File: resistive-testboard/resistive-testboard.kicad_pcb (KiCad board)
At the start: 2 copper layers, 34 parts, among them J1 Conn_01x04_Pin, Q1 PMOS, Q2 PMOS, Q3 PMOS, Q4 PMOS, Q5 PMOS, Q6 PMOS

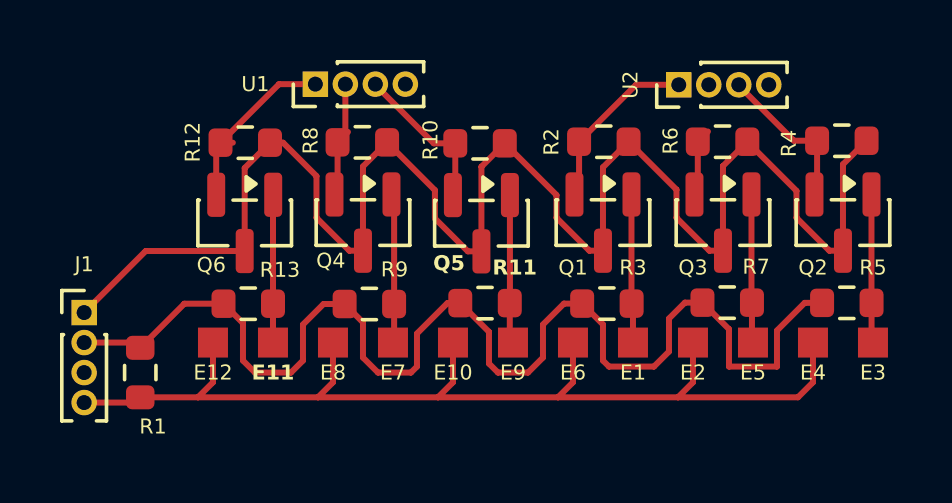
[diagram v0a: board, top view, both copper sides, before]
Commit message: fixed pinouts for ws2811 and pmos
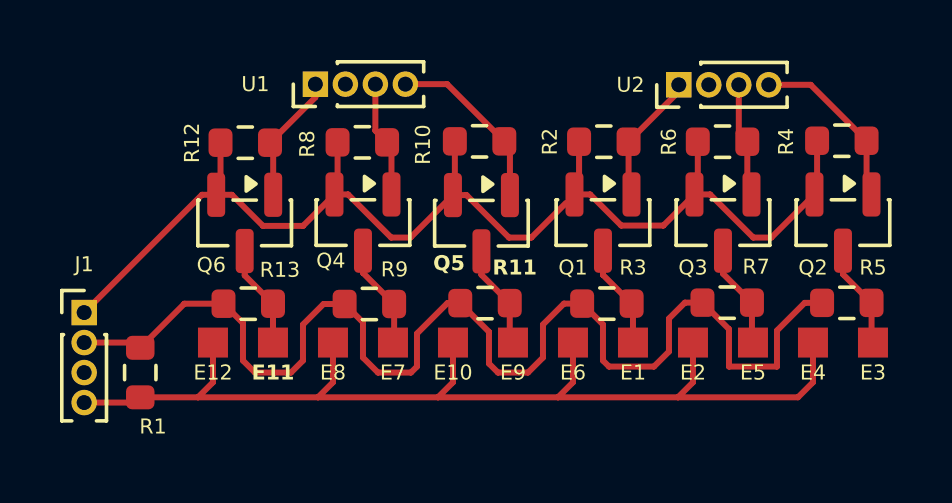
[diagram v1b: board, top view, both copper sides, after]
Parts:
- moved R10 0.07 mm to (138.9, 81.8), turned to 0 degrees
- turned R12 to 0 degrees
- turned R2 to 0 degrees
- turned R4 to 0 degrees
- turned R6 to 0 degrees
- turned R8 to 0 degrees
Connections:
- Q1 pad 1: Net-(E1-E) -> /M1/S1/SIG_IN
- Q1 pad 2: /M1/S1/SIG_IN -> /V_SIG
- Q1 pad 3: /V_SIG -> Net-(E1-E)
- Q2 pad 1: Net-(E3-E) -> /M1/S3/SIG_IN
- Q2 pad 2: /M1/S3/SIG_IN -> /V_SIG
- Q2 pad 3: /V_SIG -> Net-(E3-E)
- Q3 pad 1: Net-(E5-E) -> /M1/S2/SIG_IN
- Q3 pad 2: /M1/S2/SIG_IN -> /V_SIG
- Q3 pad 3: /V_SIG -> Net-(E5-E)
- Q4 pad 1: Net-(E7-E) -> /M2/S2/SIG_IN
- Q4 pad 2: /M2/S2/SIG_IN -> /V_SIG
- Q4 pad 3: /V_SIG -> Net-(E7-E)
- Q5 pad 1: Net-(E9-E) -> /M2/S3/SIG_IN
- Q5 pad 2: /M2/S3/SIG_IN -> /V_SIG
- Q5 pad 3: /V_SIG -> Net-(E9-E)
- Q6 pad 1: Net-(E11-E) -> /M2/S1/SIG_IN
- Q6 pad 2: /M2/S1/SIG_IN -> /V_SIG
- Q6 pad 3: /V_SIG -> Net-(E11-E)
- U1 pad 2: /M2/S2/SIG_IN -> unconnected-(U1-VDD_OUT-Pad2)
- U1 pad 3: /M2/S3/SIG_IN -> /M2/S2/SIG_IN
- U1 pad 4: unconnected-(U1-VDD_OUT-Pad4) -> /M2/S3/SIG_IN
- U2 pad 2: /M1/S2/SIG_IN -> unconnected-(U2-VDD_OUT-Pad2)
- U2 pad 3: /M1/S3/SIG_IN -> /M1/S2/SIG_IN
- U2 pad 4: unconnected-(U2-VDD_OUT-Pad4) -> /M1/S3/SIG_IN
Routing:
- net /V_SIG: track 56.2 -> 42.8 mm
- net /M2/S1/SIG_IN: track 6.33 -> 4.37 mm
- net Net-(E7-E): track 5.14 -> 3.56 mm
- net /M1/S2/SIG_IN: track 2.28 -> 3.83 mm
- net /M1/S1/SIG_IN: track 5.93 -> 4.39 mm
- net Net-(E11-E): track 6.23 -> 4.74 mm
- net Net-(E1-E): track 4.96 -> 3.48 mm
- net Net-(E5-E): track 4.96 -> 3.48 mm
- net Net-(E3-E): track 4.96 -> 3.48 mm
- net Net-(E9-E): track 5.11 -> 3.64 mm
- net /M1/S3/SIG_IN: track 5.22 -> 5.89 mm
- net /M2/S3/SIG_IN: track 5.45 -> 5.96 mm

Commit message: added pcb?
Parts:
- J1: footprint Connector_PinHeader_1.00mm:PinHeader_1x04_P1.00mm_Vertical -> Connector_PinHeader_2.54mm:PinHeader_1x04_P2.54mm_Vertical
- moved J1 3.09 mm to (124.0, 84.9)
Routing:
- net RX: track 36.3 -> 38.9 mm
- net GND: track 41.5 -> 43.6 mm
- net /V_SIG: track 42.8 -> 43.9 mm

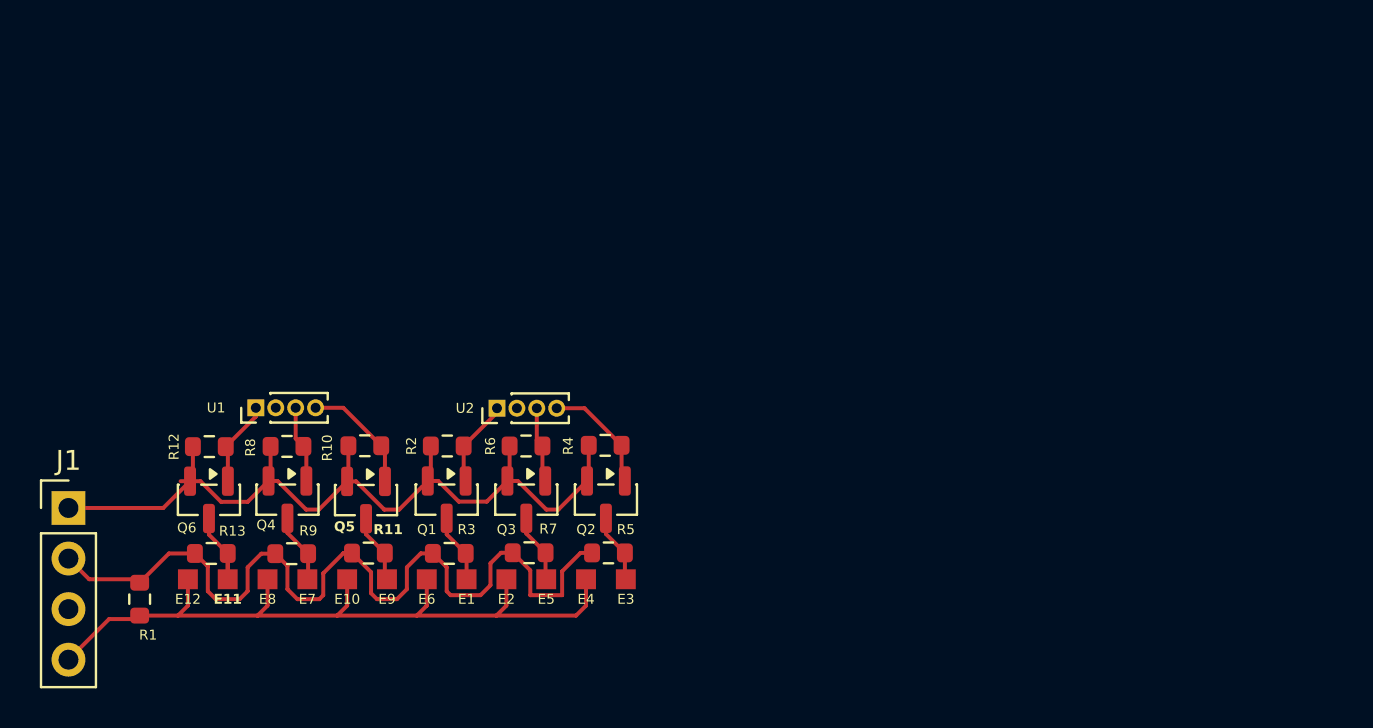
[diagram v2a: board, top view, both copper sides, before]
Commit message: moved pulldown resistor lower, added more copies of symbol
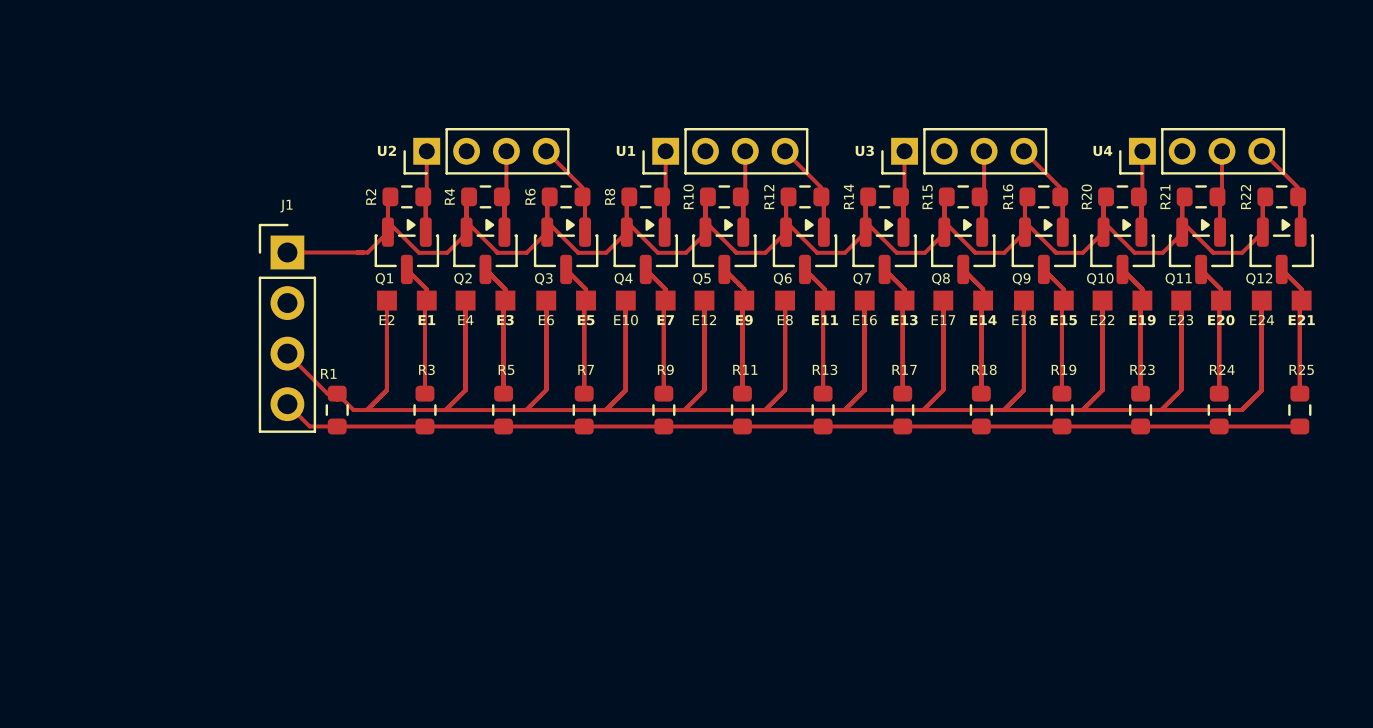
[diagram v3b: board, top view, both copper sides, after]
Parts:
- removed the E7 at (136.0, 88.5)
- removed the E8 at (134.0, 88.5)
- removed the Q4 at (135.0, 84.5)
- removed the R8 at (135.0, 81.8)
- removed the R9 at (135.2, 87.2)
- added E11: ~, fibercircuitsfps:Electrode, F.Cu at (162.0, 74.5)
- added E12: ~, fibercircuitsfps:Electrode, F.Cu at (155.9, 74.5)
- added E13: ~, fibercircuitsfps:Electrode, F.Cu at (166.0, 74.5)
- added E14: ~, fibercircuitsfps:Electrode, F.Cu at (169.9, 74.5)
- added E15: ~, fibercircuitsfps:Electrode, F.Cu at (174.0, 74.5)
- added E16: ~, fibercircuitsfps:Electrode, F.Cu at (164.0, 74.5)
- added E17: ~, fibercircuitsfps:Electrode, F.Cu at (167.9, 74.5)
- added E18: ~, fibercircuitsfps:Electrode, F.Cu at (172.0, 74.5)
- added E19: ~, fibercircuitsfps:Electrode, F.Cu at (177.9, 74.5)
- added E20: ~, fibercircuitsfps:Electrode, F.Cu at (181.9, 74.5)
- added E21: ~, fibercircuitsfps:Electrode, F.Cu at (185.9, 74.5)
- added E22: ~, fibercircuitsfps:Electrode, F.Cu at (175.9, 74.5)
- added E23: ~, fibercircuitsfps:Electrode, F.Cu at (179.9, 74.5)
- added E24: ~, fibercircuitsfps:Electrode, F.Cu at (183.9, 74.5)
- added Q10: PMOS, Package_TO_SOT_SMD:SOT-23, F.Cu at (176.9, 72.0)
- added Q11: PMOS, Package_TO_SOT_SMD:SOT-23, F.Cu at (180.9, 72.0)
- added Q12: PMOS, Package_TO_SOT_SMD:SOT-23, F.Cu at (184.9, 72.0)
- added Q6: PMOS, Package_TO_SOT_SMD:SOT-23, F.Cu at (161.0, 72.0)
- added Q7: PMOS, Package_TO_SOT_SMD:SOT-23, F.Cu at (165.0, 72.0)
- added Q8: PMOS, Package_TO_SOT_SMD:SOT-23, F.Cu at (168.9, 72.0)
- added Q9: PMOS, Package_TO_SOT_SMD:SOT-23, F.Cu at (173.0, 72.0)
- added R12: 10M, Resistor_SMD:R_0603_1608Metric, F.Cu at (161.0, 69.3)
- added R13: R, Resistor_SMD:R_0603_1608Metric, F.Cu at (161.9, 80.0)
- added R14: 10M, Resistor_SMD:R_0603_1608Metric, F.Cu at (165.0, 69.3)
- added R15: 10M, Resistor_SMD:R_0603_1608Metric, F.Cu at (168.9, 69.3)
- added R16: 10M, Resistor_SMD:R_0603_1608Metric, F.Cu at (173.0, 69.3)
- added R17: R, Resistor_SMD:R_0603_1608Metric, F.Cu at (165.9, 80.0)
- added R18: R, Resistor_SMD:R_0603_1608Metric, F.Cu at (169.9, 80.0)
- added R19: R, Resistor_SMD:R_0603_1608Metric, F.Cu at (173.9, 80.0)
- added R20: 10M, Resistor_SMD:R_0603_1608Metric, F.Cu at (176.9, 69.3)
- added R21: 10M, Resistor_SMD:R_0603_1608Metric, F.Cu at (180.9, 69.3)
- added R22: 10M, Resistor_SMD:R_0603_1608Metric, F.Cu at (184.9, 69.3)
- added R23: R, Resistor_SMD:R_0603_1608Metric, F.Cu at (177.9, 80.0)
- added R24: R, Resistor_SMD:R_0603_1608Metric, F.Cu at (181.8, 80.0)
- added R25: R, Resistor_SMD:R_0603_1608Metric, F.Cu at (185.9, 80.0)
- added U3: ~, Connector_PinHeader_2.00mm:PinHeader_1x04_P2.00mm_Vertical, F.Cu at (166.0, 67.0)
- added U4: ~, Connector_PinHeader_2.00mm:PinHeader_1x04_P2.00mm_Vertical, F.Cu at (177.9, 67.0)
- U1, U2: footprint Connector_PinHeader_1.00mm:PinHeader_1x04_P1.00mm_Vertical -> Connector_PinHeader_2.00mm:PinHeader_1x04_P2.00mm_Vertical
- moved E8 33.1 mm to (160.0, 74.5)
- moved E7 26.1 mm to (154.0, 74.5)
- moved Q4 25.3 mm to (153.0, 72.0)
- moved R8 25.3 mm to (153.0, 69.3)
- moved U1 24.3 mm to (154.0, 67.0)
- moved R9 23.8 mm to (153.9, 80.0), turned to -90 degrees
- moved E9 22.8 mm to (157.9, 74.5)
- moved R10 22.0 mm to (156.9, 69.3)
- moved Q5 21.9 mm to (156.9, 72.0)
- moved R11 20.1 mm to (157.9, 80.0), turned to -90 degrees
- moved E10 19.8 mm to (152.0, 74.5)
- moved J1 16.9 mm to (135.0, 72.1)
- moved E3 15.3 mm to (145.9, 74.5)
- moved E4 15.3 mm to (143.9, 74.5)
- moved E2 15.2 mm to (140.0, 74.5)
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- renumbered E11 to E7, E12 to E8, Q6 to Q4, R12 to R8, R13 to R9
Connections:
- J1 pad 2: GND -> +5V
- J1 pad 3: +5V -> RX
- J1 pad 4: RX -> GND
- Q2 pad 1: /M1/S3/SIG_IN -> /M1/S2/SIG_IN
- Q3 pad 1: /M1/S2/SIG_IN -> /M1/S3/SIG_IN
- Q5 pad 1: /M2/S3/SIG_IN -> /M2/S2/SIG_IN
- R10 pad 2: /M2/S3/SIG_IN -> /M2/S2/SIG_IN
- R4 pad 2: /M1/S3/SIG_IN -> /M1/S2/SIG_IN
- R6 pad 2: /M1/S2/SIG_IN -> /M1/S3/SIG_IN
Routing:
- net RX: track 38.9 -> 429.9 mm
- net /V_SIG: track 43.9 -> 140.5 mm
- net Net-(E21-E): track 0.00 -> 21.9 mm
- net Net-(E15-E): track 0.00 -> 21.9 mm
- net Net-(E14-E): track 0.00 -> 21.9 mm
- net Net-(E13-E): track 0.00 -> 21.9 mm
- net Net-(E11-E): track 0.00 -> 21.9 mm
- net Net-(E20-E): track 0.00 -> 21.9 mm
- net Net-(E19-E): track 0.00 -> 21.9 mm
- net Net-(E3-E): track 3.48 -> 21.9 mm
- net Net-(E1-E): track 3.48 -> 21.9 mm
- net Net-(E5-E): track 3.48 -> 21.9 mm
- net Net-(E9-E): track 3.64 -> 21.9 mm
- net Net-(E7-E): track 4.74 -> 21.9 mm
- net /M4/S3/SIG_IN: track 0.00 -> 9.27 mm
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
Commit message: added edge cuts, fixed duplicated traces
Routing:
- net RX: track 429.9 -> 125.4 mm
- net /V_SIG: track 140.5 -> 100.3 mm
- net Net-(E21-E): track 21.9 -> 8.93 mm
- net Net-(E15-E): track 21.9 -> 8.93 mm
- net Net-(E14-E): track 21.9 -> 8.93 mm
- net Net-(E1-E): track 21.9 -> 8.93 mm
- net Net-(E3-E): track 21.9 -> 8.93 mm
- net Net-(E13-E): track 21.9 -> 8.93 mm
- net Net-(E11-E): track 21.9 -> 8.93 mm
- net Net-(E9-E): track 21.9 -> 8.93 mm
- net Net-(E7-E): track 21.9 -> 8.93 mm
- net Net-(E20-E): track 21.9 -> 8.93 mm
- net Net-(E19-E): track 21.9 -> 8.93 mm
- net Net-(E5-E): track 21.9 -> 8.93 mm
- net /M3/S1/SIG_IN: track 8.81 -> 5.52 mm
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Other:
- board outline added: 55 x 17.6 mm

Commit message: physically isolated electrodes for easier touching
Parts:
- moved Q1 2.06 mm to (141.0, 69.9)
- moved Q10 2.06 mm to (176.9, 69.9)
- moved Q11 2.06 mm to (180.9, 69.9)
- moved Q12 2.06 mm to (184.9, 69.9)
- moved Q2 2.06 mm to (144.9, 69.9)
- moved Q3 2.06 mm to (149.0, 69.9)
- moved Q4 2.06 mm to (153.0, 69.9)
- moved Q5 2.06 mm to (156.9, 69.9)
- moved Q6 2.06 mm to (161.0, 69.9)
- moved Q7 2.06 mm to (165.0, 69.9)
- moved Q8 2.06 mm to (168.9, 69.9)
- moved Q9 2.06 mm to (173.0, 69.9)
- moved R10 2.06 mm to (156.9, 67.2)
- moved R12 2.06 mm to (161.0, 67.2)
- moved R14 2.06 mm to (165.0, 67.2)
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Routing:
- net /V_SIG: track 100.3 -> 93.6 mm
- net RX: track 125.4 -> 120.9 mm
- net /M4/S2/SIG_IN: track 5.53 -> 7.89 mm
- net /M1/S2/SIG_IN: track 5.53 -> 7.89 mm
- net /M3/S2/SIG_IN: track 5.53 -> 7.89 mm
- net /M2/S2/SIG_IN: track 5.53 -> 7.89 mm
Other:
- board size 55 x 17.6 mm -> 55 x 19.6 mm

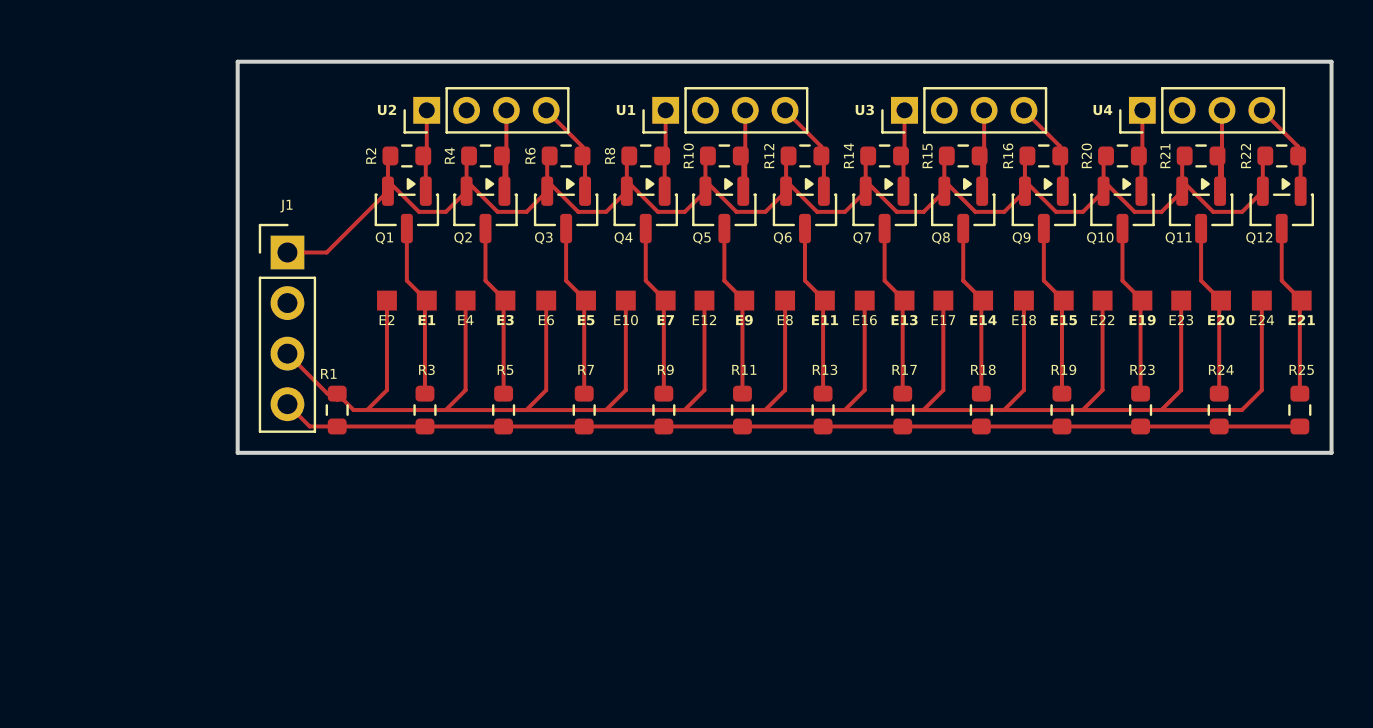
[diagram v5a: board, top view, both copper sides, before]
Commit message: moved electrodes even farther away
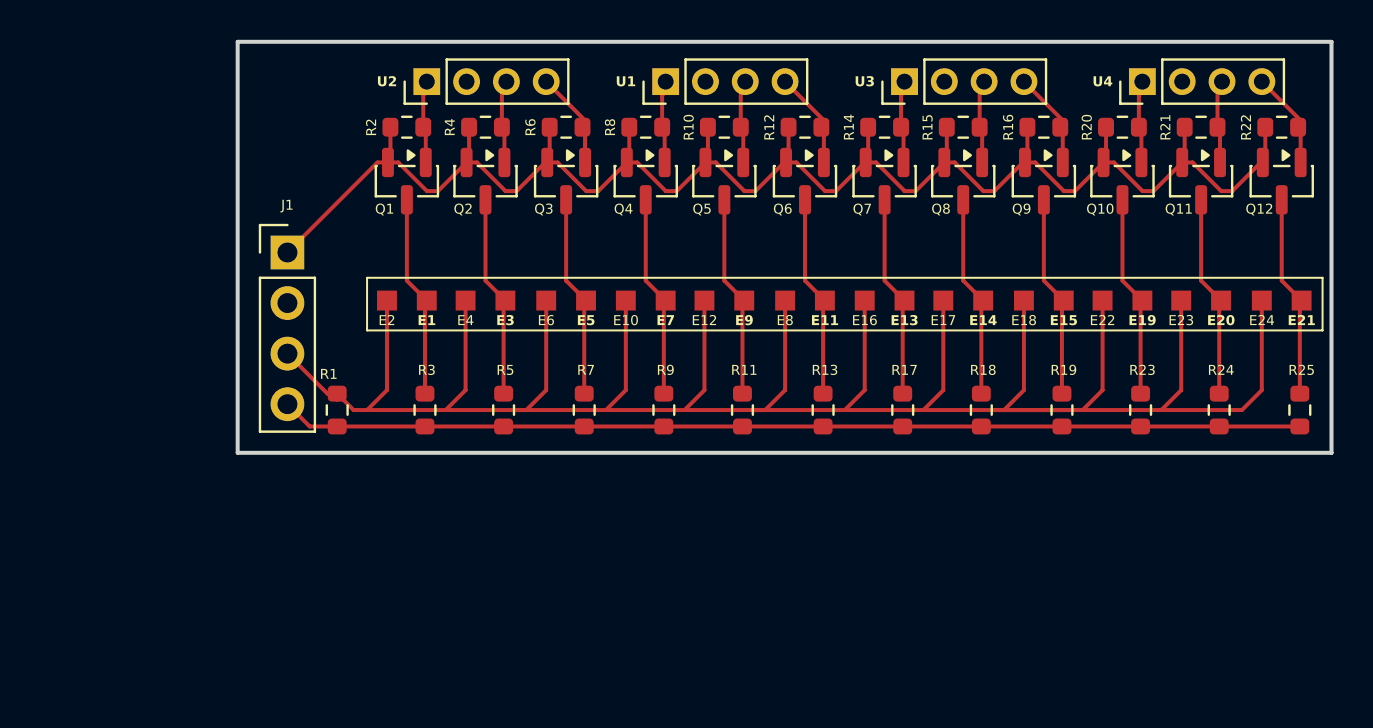
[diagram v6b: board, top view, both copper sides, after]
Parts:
- moved Q1 1.44 mm to (141.0, 68.5)
- moved Q10 1.44 mm to (176.9, 68.5)
- moved Q11 1.44 mm to (180.9, 68.5)
- moved Q12 1.44 mm to (184.9, 68.5)
- moved Q2 1.44 mm to (144.9, 68.5)
- moved Q3 1.44 mm to (149.0, 68.5)
- moved Q4 1.44 mm to (153.0, 68.5)
- moved Q5 1.44 mm to (156.9, 68.5)
- moved Q6 1.44 mm to (161.0, 68.5)
- moved Q7 1.44 mm to (165.0, 68.5)
- moved Q8 1.44 mm to (168.9, 68.5)
- moved Q9 1.44 mm to (173.0, 68.5)
- moved R10 1.44 mm to (156.9, 65.8)
- moved R12 1.44 mm to (161.0, 65.8)
- moved R14 1.44 mm to (165.0, 65.8)
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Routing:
- net /V_SIG: track 93.6 -> 85.9 mm
- net RX: track 120.9 -> 125.4 mm
- net /M4/S2/SIG_IN: track 7.89 -> 4.21 mm
- net /M2/S2/SIG_IN: track 7.89 -> 4.21 mm
- net /M1/S2/SIG_IN: track 7.89 -> 4.21 mm
- net /M3/S2/SIG_IN: track 7.89 -> 4.21 mm
- net Net-(E13-E): track 9.30 -> 10.7 mm
- net Net-(E11-E): track 9.30 -> 10.7 mm
- net Net-(E9-E): track 9.30 -> 10.7 mm
- net Net-(E7-E): track 9.30 -> 10.7 mm
- net Net-(E5-E): track 9.30 -> 10.7 mm
- net Net-(E3-E): track 9.30 -> 10.7 mm
- net Net-(E21-E): track 9.30 -> 10.7 mm
- net Net-(E20-E): track 9.30 -> 10.7 mm
- net Net-(E19-E): track 9.30 -> 10.7 mm
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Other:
- board size 55 x 19.6 mm -> 55 x 20.6 mm
